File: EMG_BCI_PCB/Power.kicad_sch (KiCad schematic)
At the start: 31 parts, among them Q1 Q_PNP_Darlington_BEC, U6 TC1044S, U7 LM2776

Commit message: More schematic changes
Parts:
- removed C28, C31: 10uF, Capacitor_SMD:C_0805_2012Metric_Pad1.15x1.40mm_HandSolder, symbol Device:C
- removed C33, C34, C35: 33u, Capacitor_SMD:C_1206_3216Metric_Pad1.42x1.75mm_HandSolder, symbol Device:C
- removed FB1, FB2: Ferrite_Bead, Resistor_SMD:R_0805_2012Metric_Pad1.15x1.40mm_HandSolder, symbol Device:Ferrite_Bead
- removed Q1: Q_PNP_Darlington_BEC, symbol Device:Q_PNP_Darlington_BEC
- removed R22, R23, R26, R27, R28, R30, R31: 0, Resistor_SMD:R_0805_2012Metric_Pad1.15x1.40mm_HandSolder, symbol Device:R
- removed R29: 1000, Resistor_SMD:R_0805_2012Metric_Pad1.15x1.40mm_HandSolder, symbol Device:R
- removed R32: 10K, Resistor_SMD:R_0805_2012Metric_Pad1.15x1.40mm_HandSolder, symbol Device:R
- removed U6: TC1044S, Package_SO:SOIC-8_3.9x4.9mm_P1.27mm, symbol EMG_Circuit:TC1044S
- added C1: 1uF, Capacitor_SMD:C_0603_1608Metric_Pad1.05x0.95mm_HandSolder, symbol Device:C
- added C2: 1 nF, Capacitor_SMD:C_0603_1608Metric_Pad1.05x0.95mm_HandSolder, symbol Device:C
- added L2: INDUCTOR, Resistor_SMD:R_1210_3225Metric_Pad1.42x2.65mm_HandSolder, symbol pspice:INDUCTOR
- added TP6: TestPoint, Connector_PinHeader_2.54mm:PinHeader_1x01_P2.54mm_Vertical, symbol Connector:TestPoint
- added U5: MCP1727-3302xSN, Package_SO:SOIC-8_3.9x4.9mm_P1.27mm, symbol Regulator_Linear:MCP1727-3302xSN
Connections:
- net WGND is gone; now on net Earth: C25.2
- net Earth: now also C1.2, C2.2, U5.4 (GND)
- net Vin+: now also L2.1; no longer C25.1
- net at C30.1, R24.1, R25.1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: now also L1.1
- net at C32.1, C36.1, C37.1: now also L1.2; no longer L1.1
- new net: C1.1, C25.1, L2.2, U5.1 (Vin), U5.2 (Vin), U5.3 (~{SHDN})
- new net: TP6.1, U5.5 (PWRGD)
- new net: C2.1, U5.6 (Cdelay)
- new net: U5.7 (Sense), U5.8 (Vout)
- no-connect marks 2 -> 0
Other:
- moved on the sheet: C25, L1

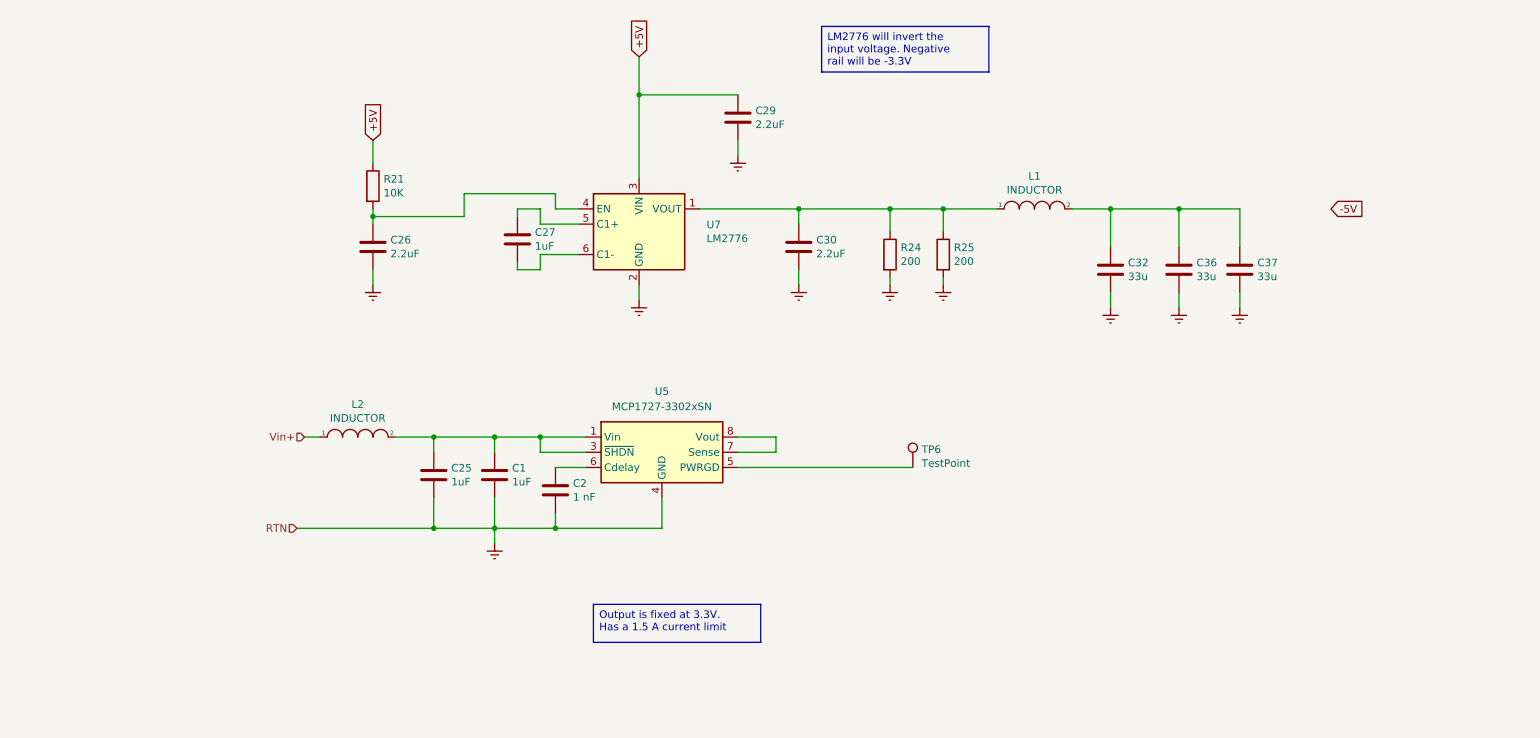
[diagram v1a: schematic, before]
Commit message: Added power symbols for +/-3.3V
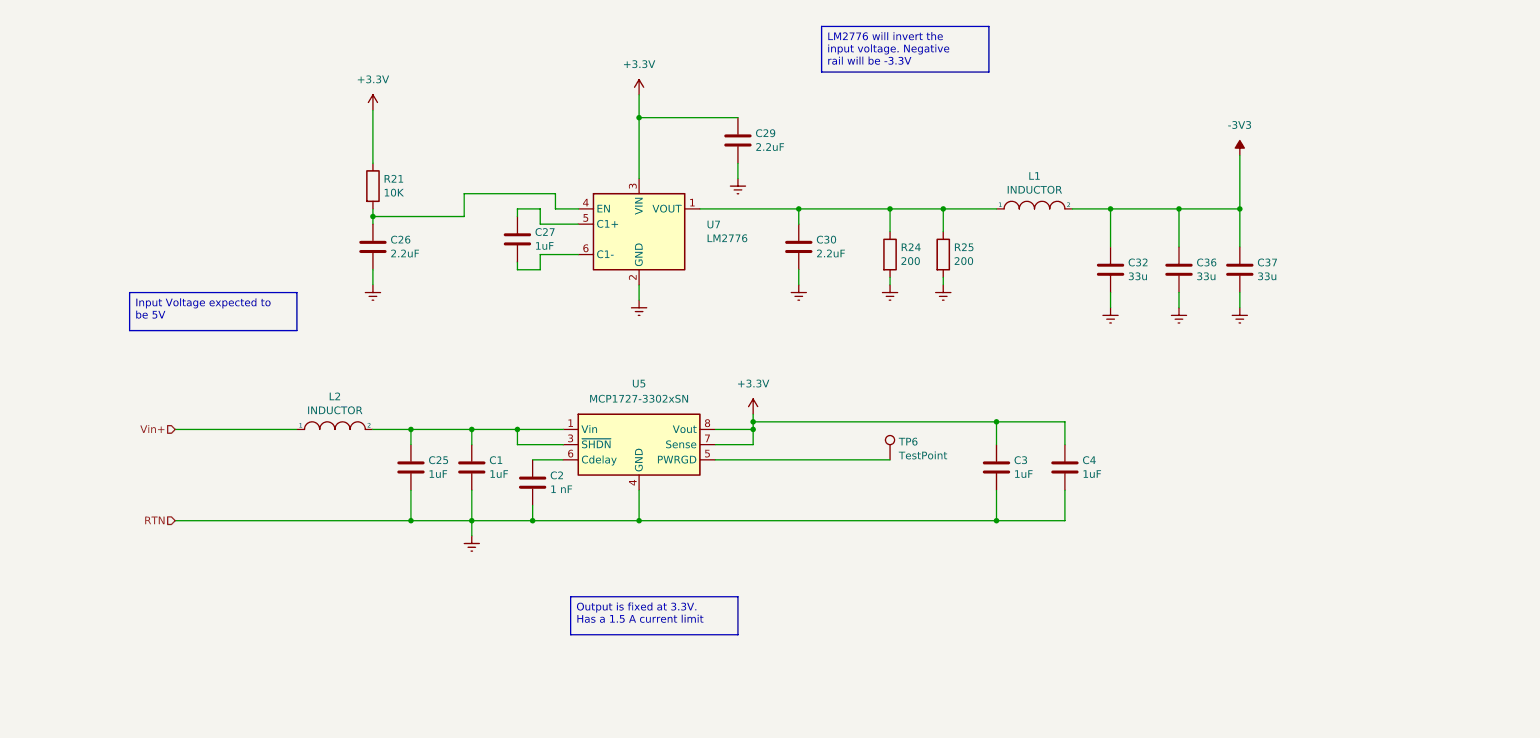
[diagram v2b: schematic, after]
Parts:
- added C3, C4: 1uF, Capacitor_SMD:C_0603_1608Metric_Pad1.05x0.95mm_HandSolder, symbol Device:C
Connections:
- net +5V is gone; now on net +3.3V: C29.1, R21.1, U7.3 (VIN)
- net Earth: now also C3.2, C4.2
- net -3V3: now reaches C32.1, C36.1, C37.1, L1.2
- net +3.3V: now reaches U5.7 (Sense), U5.8 (Vout)
- net +3.3V: now also C3.1, C4.1
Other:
- moved on the sheet: C1, C2, C25, C29, L2, TP6, U5

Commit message: Removed some warnings from the electrical rules
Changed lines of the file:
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@@
 	(text_box "Input Voltage expected to be 5V"
 		(exclude_from_sim no)
-		(at 33.02 72.39 0)
+		(at 29.21 118.11 0)
 		(size 27.94 6.35)
 		(margins 0.9525 0.9525 0.9525 0.9525)
@@
 	(text_box "Output is fixed at 3.3V. Has a 1.5 A current limit"
 		(exclude_from_sim no)
-		(at 106.68 123.19 0)
+		(at 105.41 118.11 0)
 		(size 27.94 6.35)
 		(margins 0.9525 0.9525 0.9525 0.9525)

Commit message: Assigned footprints to components
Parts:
- C1, C2, C25, C26, C27, C29, C3, C30, C4: footprint Capacitor_SMD:C_0603_1608Metric_Pad1.05x0.95mm_HandSolder -> Capacitor_SMD:C_0201_0603Metric_Pad0.64x0.40mm_HandSolder
- C32, C36, C37: footprint Capacitor_SMD:C_1206_3216Metric_Pad1.42x1.75mm_HandSolder -> Capacitor_SMD:C_0201_0603Metric_Pad0.64x0.40mm_HandSolder
- R21, R24, R25: footprint Resistor_SMD:R_0805_2012Metric_Pad1.15x1.40mm_HandSolder -> Resistor_SMD:R_0603_1608Metric_Pad0.98x0.95mm_HandSolder
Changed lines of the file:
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@@
 			)
 		)
-		(property "Footprint" "Capacitor_SMD:C_0603_1608Metric_Pad1.05x0.95mm_HandSolder"
+		(property "Footprint" "Capacitor_SMD:C_0201_0603Metric_Pad0.64x0.40mm_HandSolder"
 			(at 98.7552 67.31 0)
 			(effects
@@
 			)
 		)
-		(property "Footprint" "Capacitor_SMD:C_0603_1608Metric_Pad1.05x0.95mm_HandSolder"
+		(property "Footprint" "Capacitor_SMD:C_0201_0603Metric_Pad0.64x0.40mm_HandSolder"
 			(at 74.6252 68.58 0)
 			(effects
@@
 			)
 		)
-		(property "Footprint" "Resistor_SMD:R_0805_2012Metric_Pad1.15x1.40mm_HandSolder"
+		(property "Footprint" "Resistor_SMD:R_0603_1608Metric_Pad0.98x0.95mm_HandSolder"
 			(at 71.882 54.61 90)
 			(effects
@@
 			)
 		)
-		(property "Footprint" "Capacitor_SMD:C_0603_1608Metric_Pad1.05x0.95mm_HandSolder"
+		(property "Footprint" "Capacitor_SMD:C_0201_0603Metric_Pad0.64x0.40mm_HandSolder"
 			(at 135.5852 50.8 0)
 			(effects
@@
 			)
 		)
-		(property "Footprint" "Capacitor_SMD:C_0603_1608Metric_Pad1.05x0.95mm_HandSolder"
+		(property "Footprint" "Capacitor_SMD:C_0201_0603Metric_Pad0.64x0.40mm_HandSolder"
 			(at 145.7452 68.58 0)
 			(effects
@@
 			)
 		)
-		(property "Footprint" "Resistor_SMD:R_0805_2012Metric_Pad1.15x1.40mm_HandSolder"
+		(property "Footprint" "Resistor_SMD:R_0603_1608Metric_Pad0.98x0.95mm_HandSolder"
 			(at 158.242 66.04 90)
 			(effects
@@
 			)
 		)
-		(property "Footprint" "Resistor_SMD:R_0805_2012Metric_Pad1.15x1.40mm_HandSolder"
+		(property "Footprint" "Resistor_SMD:R_0603_1608Metric_Pad0.98x0.95mm_HandSolder"
 			(at 167.132 66.04 90)
 			(effects
@@
 			)
 		)
-		(property "Footprint" "Capacitor_SMD:C_0603_1608Metric_Pad1.05x0.95mm_HandSolder"
+		(property "Footprint" "Capacitor_SMD:C_0201_0603Metric_Pad0.64x0.40mm_HandSolder"
 			(at 80.9752 105.41 0)
 			(effects
@@
 			)
 		)
-		(property "Footprint" "Capacitor_SMD:C_1206_3216Metric_Pad1.42x1.75mm_HandSolder"
+		(property "Footprint" "Capacitor_SMD:C_0201_0603Metric_Pad0.64x0.40mm_HandSolder"
 			(at 197.8152 72.39 0)
 			(effects
@@
 			)
 		)
-		(property "Footprint" "Capacitor_SMD:C_1206_3216Metric_Pad1.42x1.75mm_HandSolder"
+		(property "Footprint" "Capacitor_SMD:C_0201_0603Metric_Pad0.64x0.40mm_HandSolder"
 			(at 209.2452 72.39 0)
 			(effects
@@
 			)
 		)
-		(property "Footprint" "Capacitor_SMD:C_1206_3216Metric_Pad1.42x1.75mm_HandSolder"
+		(property "Footprint" "Capacitor_SMD:C_0201_0603Metric_Pad0.64x0.40mm_HandSolder"
 			(at 219.4052 72.39 0)
 			(effects
@@
 			)
 		)
-		(property "Footprint" "Capacitor_SMD:C_0603_1608Metric_Pad1.05x0.95mm_HandSolder"
+		(property "Footprint" "Capacitor_SMD:C_0201_0603Metric_Pad0.64x0.40mm_HandSolder"
 			(at 190.1952 105.41 0)
 			(effects
@@
 			)
 		)
-		(property "Footprint" "Capacitor_SMD:C_0603_1608Metric_Pad1.05x0.95mm_HandSolder"
+		(property "Footprint" "Capacitor_SMD:C_0201_0603Metric_Pad0.64x0.40mm_HandSolder"
 			(at 101.2952 107.95 0)
 			(effects
@@
 			)
 		)
-		(property "Footprint" "Capacitor_SMD:C_0603_1608Metric_Pad1.05x0.95mm_HandSolder"
+		(property "Footprint" "Capacitor_SMD:C_0201_0603Metric_Pad0.64x0.40mm_HandSolder"
 			(at 91.1352 105.41 0)
 			(effects
@@
 			)
 		)
-		(property "Footprint" "Capacitor_SMD:C_0603_1608Metric_Pad1.05x0.95mm_HandSolder"
+		(property "Footprint" "Capacitor_SMD:C_0201_0603Metric_Pad0.64x0.40mm_HandSolder"
 			(at 178.7652 105.41 0)
 			(effects

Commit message: Removed inductors on power lines
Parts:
- removed L1, L2: INDUCTOR, Resistor_SMD:R_1210_3225Metric_Pad1.42x2.65mm_HandSolder, symbol pspice:INDUCTOR
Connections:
- net -3V3: now also C30.1, R24.1, R25.1, U7.1 (VOUT)
- net Vin+: now also C1.1, C25.1, U5.1 (Vin), U5.2 (Vin), U5.3 (~{SHDN})
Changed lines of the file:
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@@
-	(wire
-		(pts
-			(xy 73.66 95.25) (xy 80.01 95.25)
-		)
-		(stroke
-			(width 0)
-			(type default)
-		)
-	)
 	(wire
 		(pts
@@
 	(wire
 		(pts
-			(xy 40.64 95.25) (xy 60.96 95.25)
+			(xy 40.64 95.25) (xy 80.01 95.25)
 		)
 		(stroke
@@
 	(wire
 		(pts
-			(xy 168.91 58.42) (xy 177.8 58.42)
+			(xy 168.91 58.42) (xy 196.85 58.42)
 		)
 		(stroke
@@
 		(pts
 			(xy 168.91 71.12) (xy 168.91 69.85)
-		)
-		(stroke
-			(width 0)
-			(type default)
-		)
-	)
-	(wire
-		(pts
-			(xy 190.5 58.42) (xy 196.85 58.42)
 		)
 		(stroke
@@
 	)
 	(symbol
-		(lib_id "pspice:INDUCTOR")
-		(at 184.15 58.42 0)
-		(unit 1)
-		(exclude_from_sim no)
-		(in_bom yes)
-		(on_board yes)
-		(dnp no)
-		(property "Reference" "L1"
-			(at 184.15 52.959 0)
-			(effects
-				(font
-					(size 1.27 1.27)
-				)
-			)
-		)
-		(property "Value" "INDUCTOR"
-			(at 184.15 55.2704 0)
-			(effects
-				(font
-					(size 1.27 1.27)
-				)
-			)
-		)
-		(property "Footprint" "Resistor_SMD:R_1210_3225Metric_Pad1.42x2.65mm_HandSolder"
-			(at 184.15 58.42 0)
-			(effects
-				(font
-					(size 1.27 1.27)
-				)
-				(hide yes)
-			)
-		)
-		(property "Datasheet" "~"
-			(at 184.15 58.42 0)
-			(effects
-				(font
-					(size 1.27 1.27)
-				)
-				(hide yes)
-			)
-		)
-		(property "Description" ""
-			(at 184.15 58.42 0)
-			(effects
-				(font
-					(size 1.27 1.27)
-				)
-			)
-		)
-		(pin "1"
-		)
-		(pin "2"
-		)
-		(instances
-			(project "EMG_BCI_PCB"
-				(path "/55cf2478-b5ba-45ce-afa6-3f75a1bb5fb4/00000000-0000-0000-0000-00005f13e62e"
-					(reference "L1")
-					(unit 1)
-				)
-			)
-		)
-	)
-	(symbol
 		(lib_id "Device:C")
 		(at 196.85 68.58 0)
@@
 					(unit 1)
 				)
-			)
-		)
-	)
-	(symbol
-		(lib_id "pspice:INDUCTOR")
-		(at 67.31 95.25 0)
-		(unit 1)
-		(exclude_from_sim no)
-		(in_bom yes)
-		(on_board yes)
-		(dnp no)
-		(property "Reference" "L2"
-			(at 67.31 89.789 0)
-			(effects
-				(font
-					(size 1.27 1.27)
-				)
-			)
-		)
-		(property "Value" "INDUCTOR"
-			(at 67.31 92.1004 0)
-			(effects
-				(font
-					(size 1.27 1.27)
-				)
-			)
-		)
-		(property "Footprint" "Resistor_SMD:R_1210_3225Metric_Pad1.42x2.65mm_HandSolder"
-			(at 67.31 95.25 0)
-			(effects
-				(font
-					(size 1.27 1.27)
-				)
-				(hide yes)
-			)
-		)
-		(property "Datasheet" "~"
-			(at 67.31 95.25 0)
-			(effects
-				(font
-					(size 1.27 1.27)
-				)
-				(hide yes)
-			)
-		)
-		(property "Description" ""
-			(at 67.31 95.25 0)
-			(effects
-				(font
-					(size 1.27 1.27)
-				)
-			)
-		)
-		(pin "1"
-		)
-		(pin "2"
-		)
-		(instances
-			(project "EMG_BCI_PCB"
-				(path "/55cf2478-b5ba-45ce-afa6-3f75a1bb5fb4/00000000-0000-0000-0000-00005f13e62e"
-					(reference "L2")
-					(unit 1)
-				)

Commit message: Initial placement and routing
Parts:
- C1, C2, C25, C26, C27, C29, C3, C30, C32, C36, C37, C4: footprint Capacitor_SMD:C_0201_0603Metric_Pad0.64x0.40mm_HandSolder -> Capacitor_SMD:C_0603_1608Metric_Pad1.08x0.95mm_HandSolder
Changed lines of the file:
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@@
 			)
 		)
-		(property "Footprint" "Capacitor_SMD:C_0201_0603Metric_Pad0.64x0.40mm_HandSolder"
+		(property "Footprint" "Capacitor_SMD:C_0603_1608Metric_Pad1.08x0.95mm_HandSolder"
 			(at 98.7552 67.31 0)
 			(effects
@@
 			)
 		)
-		(property "Footprint" "Capacitor_SMD:C_0201_0603Metric_Pad0.64x0.40mm_HandSolder"
+		(property "Footprint" "Capacitor_SMD:C_0603_1608Metric_Pad1.08x0.95mm_HandSolder"
 			(at 74.6252 68.58 0)
 			(effects
@@
 			)
 		)
-		(property "Footprint" "Capacitor_SMD:C_0201_0603Metric_Pad0.64x0.40mm_HandSolder"
+		(property "Footprint" "Capacitor_SMD:C_0603_1608Metric_Pad1.08x0.95mm_HandSolder"
 			(at 135.5852 50.8 0)
 			(effects
@@
 			)
 		)
-		(property "Footprint" "Capacitor_SMD:C_0201_0603Metric_Pad0.64x0.40mm_HandSolder"
+		(property "Footprint" "Capacitor_SMD:C_0603_1608Metric_Pad1.08x0.95mm_HandSolder"
 			(at 145.7452 68.58 0)
 			(effects
@@
 			)
 		)
-		(property "Footprint" "Capacitor_SMD:C_0201_0603Metric_Pad0.64x0.40mm_HandSolder"
+		(property "Footprint" "Capacitor_SMD:C_0603_1608Metric_Pad1.08x0.95mm_HandSolder"
 			(at 80.9752 105.41 0)
 			(effects
@@
 			)
 		)
-		(property "Footprint" "Capacitor_SMD:C_0201_0603Metric_Pad0.64x0.40mm_HandSolder"
+		(property "Footprint" "Capacitor_SMD:C_0603_1608Metric_Pad1.08x0.95mm_HandSolder"
 			(at 197.8152 72.39 0)
 			(effects
@@
 			)
 		)
-		(property "Footprint" "Capacitor_SMD:C_0201_0603Metric_Pad0.64x0.40mm_HandSolder"
+		(property "Footprint" "Capacitor_SMD:C_0603_1608Metric_Pad1.08x0.95mm_HandSolder"
 			(at 209.2452 72.39 0)
 			(effects
@@
 			)
 		)
-		(property "Footprint" "Capacitor_SMD:C_0201_0603Metric_Pad0.64x0.40mm_HandSolder"
+		(property "Footprint" "Capacitor_SMD:C_0603_1608Metric_Pad1.08x0.95mm_HandSolder"
 			(at 219.4052 72.39 0)
 			(effects
@@
 			)
 		)
-		(property "Footprint" "Capacitor_SMD:C_0201_0603Metric_Pad0.64x0.40mm_HandSolder"
+		(property "Footprint" "Capacitor_SMD:C_0603_1608Metric_Pad1.08x0.95mm_HandSolder"
 			(at 190.1952 105.41 0)
 			(effects
@@
 			)
 		)
-		(property "Footprint" "Capacitor_SMD:C_0201_0603Metric_Pad0.64x0.40mm_HandSolder"
+		(property "Footprint" "Capacitor_SMD:C_0603_1608Metric_Pad1.08x0.95mm_HandSolder"
 			(at 101.2952 107.95 0)
 			(effects
@@
 			)
 		)
-		(property "Footprint" "Capacitor_SMD:C_0201_0603Metric_Pad0.64x0.40mm_HandSolder"
+		(property "Footprint" "Capacitor_SMD:C_0603_1608Metric_Pad1.08x0.95mm_HandSolder"
 			(at 91.1352 105.41 0)
 			(effects
@@
 			)
 		)
-		(property "Footprint" "Capacitor_SMD:C_0201_0603Metric_Pad0.64x0.40mm_HandSolder"
+		(property "Footprint" "Capacitor_SMD:C_0603_1608Metric_Pad1.08x0.95mm_HandSolder"
 			(at 178.7652 105.41 0)
 			(effects
